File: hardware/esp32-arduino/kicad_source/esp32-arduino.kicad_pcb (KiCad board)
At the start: 2 copper layers, 72 x 53 mm, 52 parts, among them CN1 ARDUINO, Q1 Q_NMOS_GSD, SW1 TAST_HOR, SW2 TAST_HOR, SW3 TAST_HOR, SW4 TAST_HOR, SW5 TAST_HOR, SW6 TAST_HOR, U1 LT1117, U2 TLV733P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

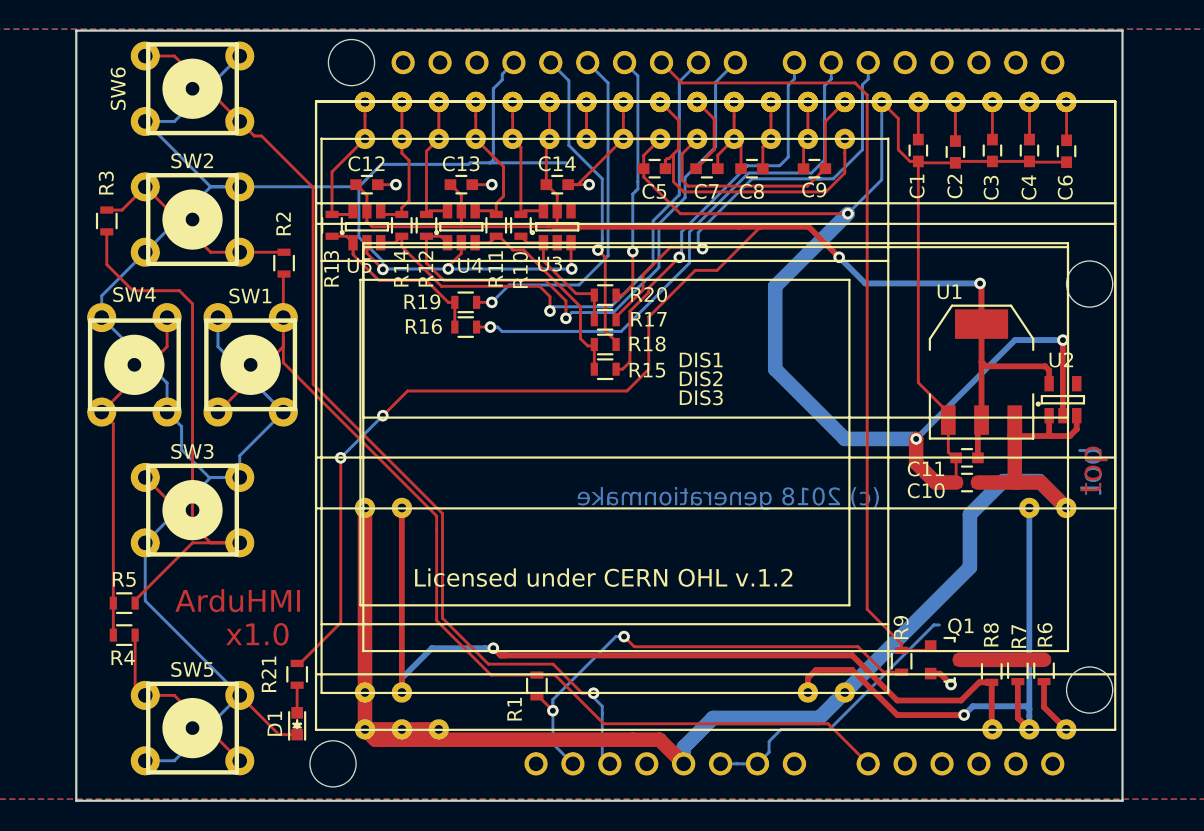
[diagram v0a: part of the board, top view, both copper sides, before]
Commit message: started schematic added ESP32
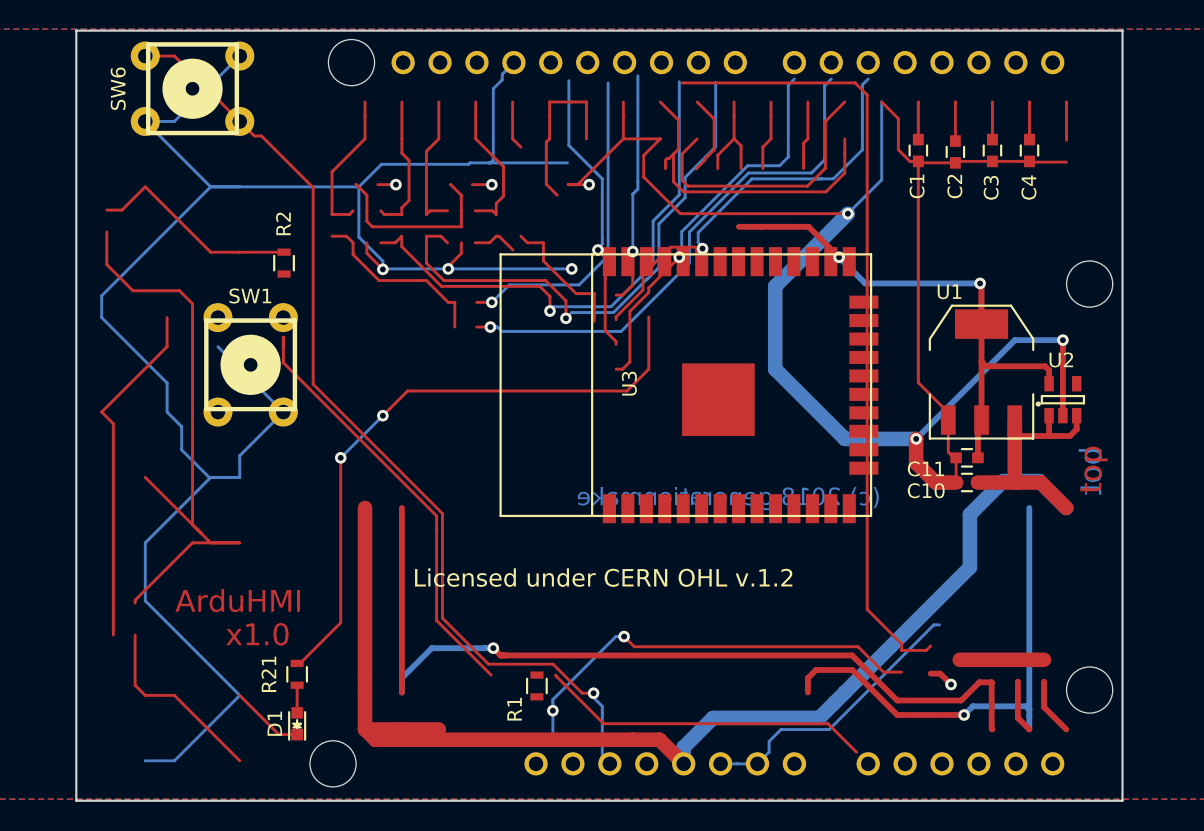
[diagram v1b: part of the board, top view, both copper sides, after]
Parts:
- removed C12, C13, C14: 100n, capacitors:C_0603
- removed C5, C6, C7, C8, C9: 1u, capacitors:C_0603
- removed DIS1: EA_DOGM128-6, displays:EA_DOGM128
- removed DIS2: EA_DOGM132-5, displays:EA_DOGM081_162_163_132
- removed DIS3: EA_DOGS102-6, displays:EA_DOGS102
- removed Q1: Q_NMOS_GSD, SOT_TO:SOT-23
- removed R10, R11, R12, R13, R14, R15, R16, R17: DNI, resistors:R_0603
- removed R18, R19, R20: 0R, resistors:R_0603
- removed R3: 620, resistors:R_0603
- removed R4, R9: 1k, resistors:R_0603
- removed R5: 3k3, resistors:R_0603
- removed R6, R7, R8: 30, resistors:R_0603
- removed SW2, SW3, SW4, SW5: TAST_HOR, mechanical-switches:PCB_PUSH
- removed U4, U5: SN74LVC2G34, SOT_TO:SOT-23-6
- C1, C2, C4: value 1u -> 100n
- C3: value 1u -> 10u
- R1: value 2k -> 1k
- R2: value 330 -> 1k
- SW1: value TAST_HOR -> SW_PUSH
- U3: value SN74LVC2G34 -> ESP32_WROOM_32; footprint SOT_TO:SOT-23-6 -> MODULE_compute:ESP32-WROOM-32
- moved U3 15.6 mm to (95.2, 101.4)
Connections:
- C1 pad 1: /DIS_V4 -> /RESET
- C10 pad 1: +5V -> VIN
- C2 pad 1: /DIS_V3 -> +3V3
- C3 pad 1: /DIS_V2 -> +3V3
- C4 pad 1: /DIS_V1 -> +3V3
- CN1 pad 0: Net-(CN1-Pad0) -> (no net)
- CN1 pad 1: Net-(CN1-Pad1) -> (no net)
- CN1 pad 10: /DISPLAY_BL -> (no net)
- CN1 pad 11: /ARDU_SI_1 -> (no net)
- CN1 pad 12: /ARDU_CS_1 -> (no net)
- CN1 pad 13: /ARDU_CLK_1 -> (no net)
- CN1 pad 15: Net-(CN1-Pad15) -> (no net)
- CN1 pad 16: Net-(CN1-Pad16) -> (no net)
- CN1 pad 17: Net-(CN1-Pad17) -> (no net)
- CN1 pad 18: /ENC_SW -> (no net)
- CN1 pad 19: /ENC_B -> (no net)
- CN1 pad 2: Net-(CN1-Pad2) -> (no net)
- CN1 pad 20: /ENC_A -> (no net)
- CN1 pad 21: Net-(CN1-Pad21) -> (no net)
- CN1 pad 22: Net-(CN1-Pad22) -> (no net)
- CN1 pad 23: /KEYPAD_A0 -> (no net)
- CN1 pad 27: +5V -> Net-(CN1-Pad27)
- CN1 pad 28: Net-(CN1-Pad28) -> +3V3
- CN1 pad 3: Net-(CN1-Pad3) -> (no net)
- CN1 pad 30: VIO -> +3V3
- CN1 pad 31: Net-(CN1-Pad31) -> (no net)
- CN1 pad 4: Net-(CN1-Pad4) -> (no net)
- CN1 pad 5: /ARDU_SI_2 -> (no net)
- CN1 pad 6: /ARDU_CS_2 -> (no net)
- CN1 pad 7: /ARDU_CLK_2 -> (no net)
- CN1 pad 8: /ARDU_A0 -> (no net)
- CN1 pad 9: /ARDU_RESET -> (no net)
- R1 pad 1: VIO -> /RESET
- R1 pad 2: /KEYPAD_A0 -> +3V3
- R2 pad 1: /KEYPAD_A0 -> Net-(CN1-Pad27)
- R2 pad 2: /BUTTON_UP -> VIN
- SW1 pad 1: GND -> /BOOT
- SW1 pad 3: /KEYPAD_A0 -> (no net)
- SW1 pad 4: /KEYPAD_A0 -> (no net)
- U1 pad 3: +5V -> VIN
- U2 pad 1: +5V -> VIN
- U2 pad 3: +5V -> VIN
- U2 pad 4: Net-(U2-Pad4) -> (no net)
- U3 pad 1: /ARDU_SI -> GND
- U3 pad 2: GND -> +3V3
- U3 pad 3: GND -> /RESET
- U3 pad 4: Net-(U3-Pad4) -> (no net)
- U3 pad 5: +3V3 -> (no net)
- U3 pad 6: /DIS_SI -> (no net)
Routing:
- net +5V: track 118.3 -> 0.00 mm
- net (no net): track 0.00 -> 108.1 mm, vias 0 -> 3
- net Net-(CN1-Pad27): track 0.00 -> 100.3 mm
- net +3V3: track 162.7 -> 109.1 mm
- net VIN: track 0.32 -> 33.0 mm
- net /ARDU_SI_2: track 30.2 -> 0.00 mm, vias 1 -> 0
- net /ARDU_CLK_2: track 27.9 -> 0.00 mm, vias 1 -> 0
- net GND: track 302.4 -> 326.8 mm, vias 10 -> 11
- net /ARDU_CLK_1: track 21.6 -> 0.00 mm, vias 1 -> 0
- net /DIS_CAP2N: track 18.9 -> 0.00 mm
- net /ARDU_SI_1: track 17.3 -> 0.00 mm, vias 1 -> 0
- net /KEYPAD_A0: track 69.1 -> 52.8 mm
- net /BUTTON_UP: track 14.7 -> 0.00 mm
- net /ARDU_CLK: track 14.5 -> 3.18 mm
- net /ARDU_SI: track 9.32 -> 0.00 mm
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
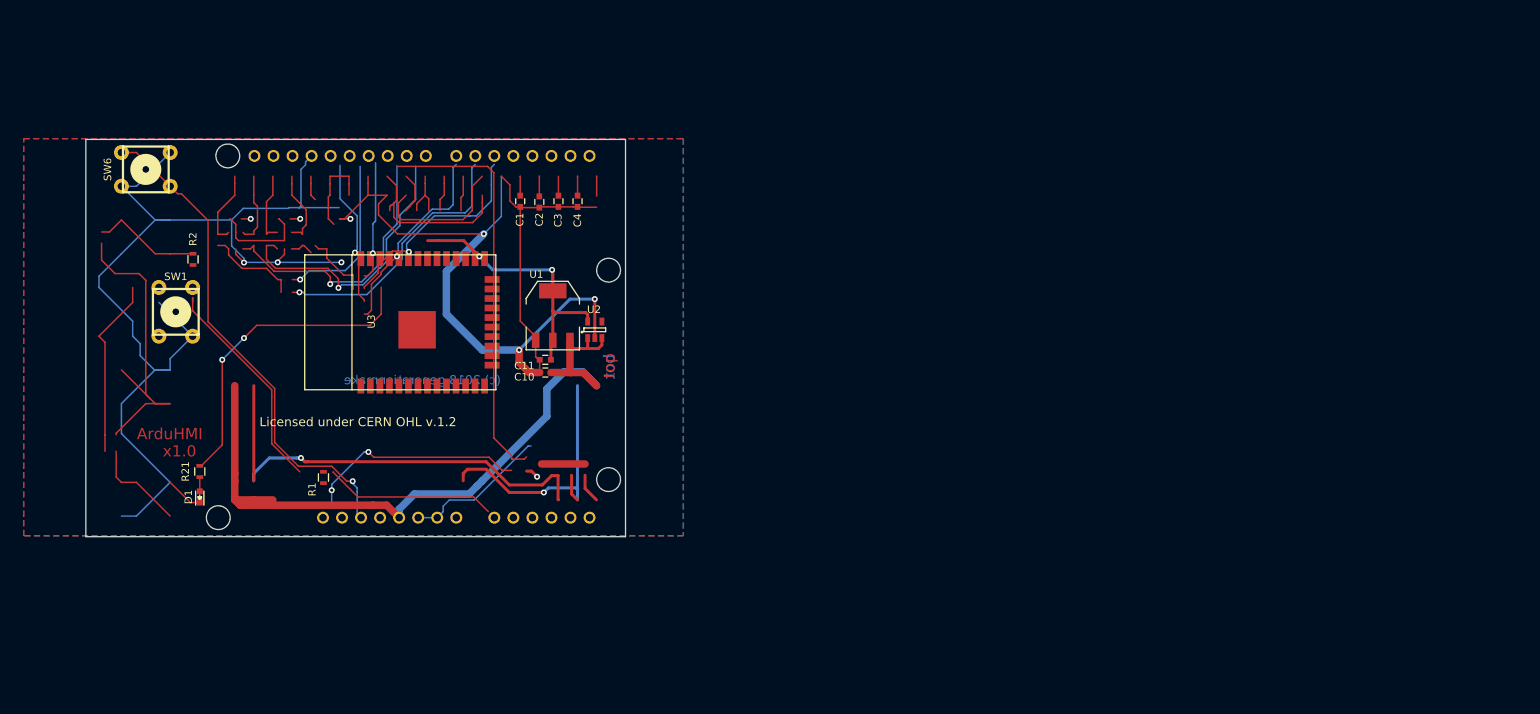
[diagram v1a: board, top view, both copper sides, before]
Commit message: corrected schematic, updated layout
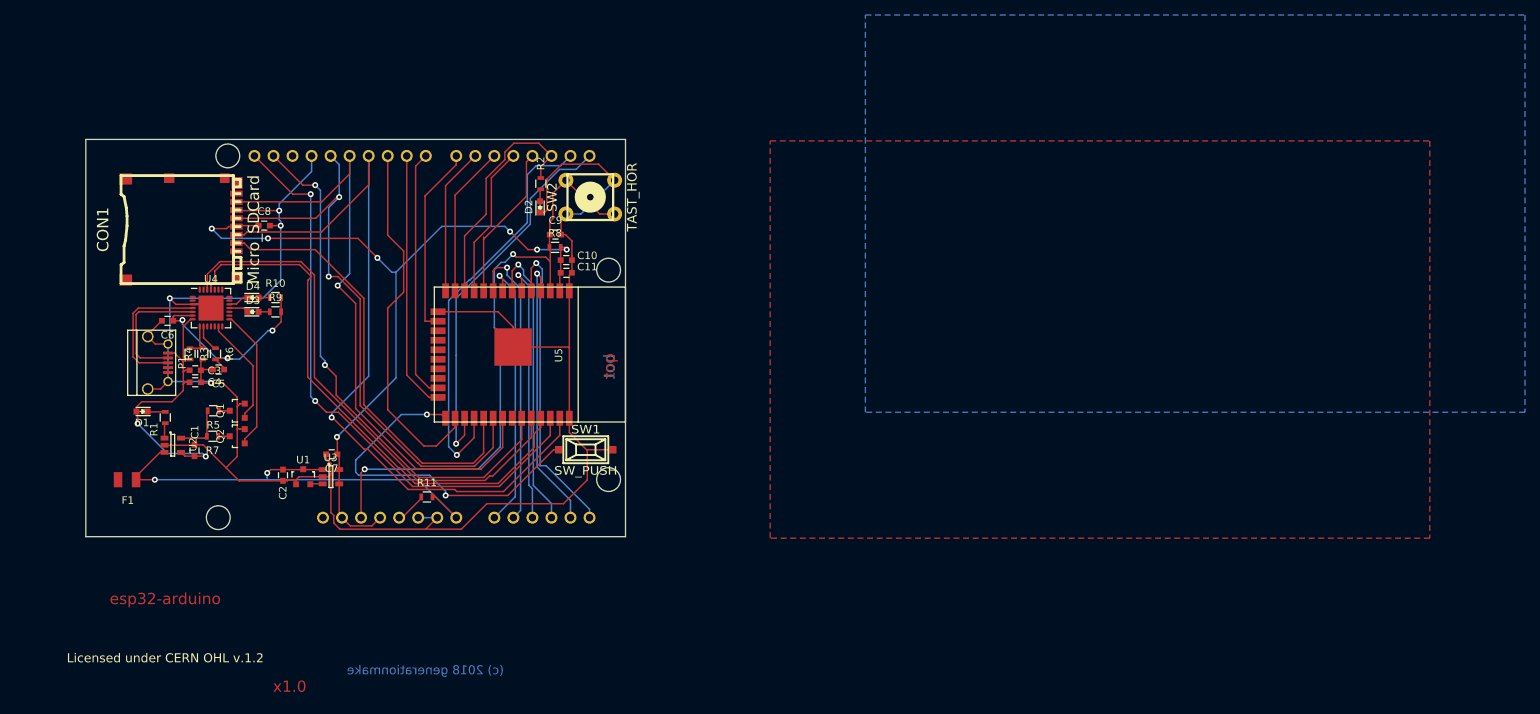
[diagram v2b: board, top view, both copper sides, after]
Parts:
- removed R21: 1k, resistors:R_0603
- removed SW6: TAST_HOR, mechanical-switches:PCB_PUSH
- added C5: 10u, capacitors:C_0603, F.Cu at (68.7, 107.7)
- added C6: 100n, capacitors:C_0603, F.Cu at (61.9, 101.2)
- added C7: 1u, capacitors:C_0603, F.Cu at (83.8, 119.0)
- added C8: 100n, capacitors:C_0603, F.Cu at (74.8, 88.5)
- added C9: 100n, capacitors:C_0603, F.Cu at (113.7, 89.7)
- added CON1: Micro_SDCard, mechanical-connectors:microsd_socket, F.Cu at (63.3, 90.6)
- added D2: green, LEDs:LED_0603, F.Cu at (111.6, 86.0)
- added D3: green, LEDs:LED_0603, F.Cu at (73.3, 100.0)
- added D4: green, LEDs:LED_0603, F.Cu at (73.3, 98.1)
- added F1: F_Small, fuse_holders_and_fuses:Fuse_SMD1206_Reflow, F.Cu at (56.5, 122.4)
- added P1: USB_OTG, mechanical-connectors:USB_Micro-B, F.Cu at (60.4, 106.8)
- added Q1: Q_NMOS_GSD, SOT_TO:SOT-23, F.Cu at (71.2, 113.2)
- added Q2: Q_NMOS_GSD, SOT_TO:SOT-23, F.Cu at (71.2, 116.6)
- added R10: 1k, resistors:R_0603, F.Cu at (76.3, 98.1)
- added R11: 1k, resistors:R_0603, F.Cu at (96.5, 124.7)
- added R3: 22k1, resistors:R_0603, F.Cu at (64.9, 105.6)
- added R4: 47k5, resistors:R_0603, F.Cu at (66.6, 105.6)
- added R5: 1k, resistors:R_0603, F.Cu at (68.0, 113.2)
- added R6: 1k, resistors:R_0603, F.Cu at (68.3, 105.6)
- added R7: 1k, resistors:R_0603, F.Cu at (67.9, 116.6)
- added R8: 1k, resistors:R_0603, F.Cu at (113.6, 91.4)
- added R9: 1k, resistors:R_0603, F.Cu at (76.3, 100.0)
- added SW2: TAST_HOR, mechanical-switches:PCB_PUSH, F.Cu at (118.3, 84.7)
- added U4: CP2102N_28, QFN:QFN-28-1EP_5x5mm_Pitch0.5mm, F.Cu at (67.7, 99.5)
- added U5: ESP32_WROOM_32, MODULE_compute:ESP32-WROOM-32, F.Cu at (108.0, 105.7)
- C1, C2: value 100n -> 1u
- C10: value 1u -> 10u
- C11: value 1u -> 100n
- SW1: footprint mechanical-switches:PCB_PUSH -> mechanical-switches:smd_push
- U1: value LT1117 -> TPS383X; footprint SOT_TO:SOT-223 -> SOT_TO:SOT-23
- U2: value TLV733P -> MCP73831
- U3: value ESP32_WROOM_32 -> TPS736XX; footprint MODULE_compute:ESP32-WROOM-32 -> SOT_TO:SOT-23-5
- moved U2 58.4 mm to (62.6, 117.8), turned to 0 degrees
- moved SW1 57.7 mm to (117.7, 118.4)
- moved C4 56.4 mm to (65.6, 109.4), turned to 0 degrees
- moved C1 54.7 mm to (65.5, 118.5), turned to 90 degrees
- moved C3 53.4 mm to (65.6, 107.8), turned to 0 degrees
- moved C2 50.0 mm to (77.3, 121.8)
- moved R2 47.5 mm to (111.7, 82.9)
- moved U1 39.6 mm to (80.0, 122.0)
- moved U3 23.6 mm to (83.7, 122.0), turned to 0 degrees
- moved R1 22.6 mm to (61.6, 114.1)
- moved C10 15.3 mm to (115.1, 93.1), turned to 0 degrees
- moved D1 13.8 mm to (58.5, 113.3), turned to 180 degrees
- moved C11 11.9 mm to (115.1, 94.8), turned to 0 degrees
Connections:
- C1 pad 1: /RESET -> VIN
- C10 pad 1: VIN -> +3V3
- C2 pad 1: +3V3 -> +BATT
- C3 pad 1: +3V3 -> VIN
- C4 pad 1: +3V3 -> VIN
- CN1 pad 0: (no net) -> /EXT_RX
- CN1 pad 1: (no net) -> /EXT_TX
- CN1 pad 10: (no net) -> /SPI_CS_EXT
- CN1 pad 11: (no net) -> /SPI_MOSI
- CN1 pad 12: (no net) -> /SPI_MISO
- CN1 pad 13: (no net) -> /SPI_CLK
- CN1 pad 16: (no net) -> /I2C_SDA
- CN1 pad 17: (no net) -> /I2C_SCL
- CN1 pad 18: (no net) -> /ADC_5
- CN1 pad 19: (no net) -> /ADC_4
- CN1 pad 2: (no net) -> /ARDUINO_2
- CN1 pad 20: (no net) -> /ADC_3
- CN1 pad 21: (no net) -> /ADC_2
- CN1 pad 22: (no net) -> /ADC_1
- CN1 pad 23: (no net) -> /ADC_0
- CN1 pad 24: VIN -> +BATT
- CN1 pad 3: (no net) -> /DAC_1
- CN1 pad 4: (no net) -> /DAC_2
- CN1 pad 5: (no net) -> /ARDUINO_5
- CN1 pad 6: (no net) -> /ARDUINO_6
- CN1 pad 7: (no net) -> /ARDUINO_7
- CN1 pad 8: (no net) -> /ARDUINO_8
- CN1 pad 9: (no net) -> /ARDUINO_9
- D1 pad 1: GND -> Net-(D1-Pad1)
- D1 pad 2: Net-(D1-Pad2) -> VIN
- R1 pad 1: /RESET -> Net-(R1-Pad1)
- R1 pad 2: +3V3 -> Net-(D1-Pad1)
- R2 pad 1: Net-(CN1-Pad27) -> Net-(D2-Pad2)
- R2 pad 2: VIN -> /ARDUINO_2
- U1 pad 2: +3V3 -> Net-(U1-Pad2)
- U1 pad 3: VIN -> +BATT
- U2 pad 1: VIN -> Net-(R1-Pad1)
- U2 pad 3: VIN -> +BATT
- U2 pad 4: (no net) -> VIN
- U2 pad 5: +3V3 -> Net-(R5-Pad2)
- U3 pad 1: GND -> +BATT
- U3 pad 2: +3V3 -> GND
- U3 pad 3: /RESET -> Net-(U1-Pad2)
- U3 pad 4: (no net) -> +3V3
- U3 pad 5: (no net) -> +3V3
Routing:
- net (no net): track 108.1 -> 0.00 mm, vias 3 -> 0
- net /SPI_MOSI: track 0.00 -> 101.1 mm, vias 0 -> 1
- net Net-(CN1-Pad27): track 100.3 -> 4.57 mm
- net /DIS_C1: track 84.6 -> 0.00 mm, vias 1 -> 0
- net /SPI_MISO: track 0.00 -> 82.5 mm, vias 0 -> 1
- net /I2C_SCL: track 0.00 -> 78.7 mm, vias 0 -> 2
- net /SPI_CLK: track 0.00 -> 77.7 mm, vias 0 -> 2
- net /RX: track 0.00 -> 72.7 mm
- net /TX: track 0.00 -> 72.6 mm
- net /I2C_SDA: track 0.00 -> 70.6 mm, vias 0 -> 2
- net +BATT: track 0.00 -> 63.5 mm, vias 0 -> 2
- net /SPI_CS_SD: track 0.00 -> 58.7 mm
- net GND: track 326.8 -> 270.5 mm, vias 11 -> 4
- net /EXT_TX: track 0.00 -> 54.9 mm, vias 0 -> 1
- net /DISPLAY_BL: track 54.4 -> 0.00 mm
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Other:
- board text added: "esp32-arduino"
- board text removed: "ArduHMI"

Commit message: finished layout, created gerber
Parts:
- added BT1: Battery, MECH_battery_holder:KEYSTONE_1043, B.Cu at (84.1, 115.0)
- added R12: 100R, resistors:R_0603, F.Cu at (107.3, 102.3)
- added R13: 100R, resistors:R_0603, F.Cu at (107.3, 103.7)
- added R14: 100R, resistors:R_0603, F.Cu at (107.3, 105.8)
- added R15: 100R, resistors:R_0603, F.Cu at (107.1, 108.1)
- CON1: footprint mechanical-connectors:microsd_socket -> CON_wuerth:WE_693072010801
- SW1: value SW_PUSH -> TAST_VER; footprint mechanical-switches:smd_push -> mechanical-switches:WE_430182050816
- SW2: value TAST_HOR -> TAST_VER; footprint mechanical-switches:PCB_PUSH -> mechanical-switches:WE_430182050816
- moved C10 69.3 mm to (46.3, 85.1), turned to 90 degrees
- moved C11 67.9 mm to (47.9, 85.0), turned to 90 degrees
- moved U5 51.4 mm to (58.4, 92.0), turned to 0 degrees
- moved C8 48.8 mm to (117.2, 112.7)
- moved CON1 48.1 mm to (109.3, 104.6), turned to 90 degrees
- moved SW1 42.5 mm to (75.9, 126.3)
- moved R8 36.0 mm to (86.1, 114.7), turned to 180 degrees
- moved R10 21.1 mm to (71.5, 118.6), turned to 270 degrees
- moved R9 19.8 mm to (69.6, 118.6), turned to 270 degrees
- moved D4 17.6 mm to (71.5, 115.6), turned to 270 degrees
- moved D3 16.0 mm to (69.6, 115.6), turned to 270 degrees
- moved Q1 11.6 mm to (59.8, 115.1), turned to 180 degrees
- moved P1 11.3 mm to (49.1, 107.6)
- moved U4 10.8 mm to (70.1, 110.0), turned to 270 degrees
- moved D2 10.4 mm to (121.6, 83.2)
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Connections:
- net Net-(R5-Pad2) renamed /PROG
- CON1 pad 2: /SPI_CS_SD -> /SPI_CS_SD_R
- CON1 pad 3: /SPI_MOSI -> /SPI_MOSI_R
- CON1 pad 5: /SPI_CLK -> /SPI_CLK_R
- CON1 pad 7: /SPI_MISO -> /SPI_MISO_R
- F1 pad 2: (no net) -> Net-(BT1-Pad1)
- SW2 pad 2: GND -> /RESET
- SW2 pad 3: /RESET -> GND
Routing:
- net /I2C_SCL: track 78.7 -> 11.4 mm, vias 2 -> 0
- net /ADC_4: track 36.9 -> 95.4 mm
- net /ARDUINO_2: track 31.7 -> 89.9 mm, vias 0 -> 2
- net /ADC_5: track 41.6 -> 99.4 mm
- net /DAC_1: track 21.0 -> 76.6 mm, vias 0 -> 2
- net /ADC_2: track 35.4 -> 90.8 mm
- net /ADC_1: track 39.2 -> 94.5 mm
- net /ADC_3: track 39.5 -> 94.8 mm
- net /ADC_0: track 36.5 -> 89.2 mm
- net /DAC_2: track 20.2 -> 72.0 mm, vias 0 -> 2
- net /ARDUINO_5: track 20.2 -> 69.1 mm, vias 0 -> 2
- net +3V3: track 109.2 -> 157.4 mm, vias 7 -> 3
- net /ARDUINO_6: track 19.6 -> 66.8 mm, vias 0 -> 2
- net GND: track 270.5 -> 317.3 mm, vias 4 -> 5
- net /I2C_SDA: track 70.6 -> 26.8 mm, vias 2 -> 0
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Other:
- board size 72 x 53 mm -> 78 x 53 mm
- board text added: "BOOT"
- board text added: "RESET"

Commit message: corrected schematic and layout, generated gerber
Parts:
- added R16: 1k, resistors:R_0603, F.Cu at (76.6, 111.8)
- added R17: 1k, resistors:R_0603, F.Cu at (76.6, 109.8)
- added R18: 1k, resistors:R_0603, F.Cu at (73.2, 83.3)
- added R19: 1k, resistors:R_0603, F.Cu at (77.2, 83.3)
- added R20: 1k, resistors:R_0603, F.Cu at (104.9, 125.1)
- added R21: 1k, resistors:R_0603, F.Cu at (108.1, 125.1)
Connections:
- U4 pad 25: /TX -> /TX_R
- U4 pad 26: /RX -> /RX_R
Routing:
- net +3V3: track 157.4 -> 192.1 mm, vias 3 -> 4
- net GND: track 317.3 -> 305.0 mm, vias 5 -> 24
- net /TX: track 50.3 -> 44.8 mm
- net /RX: track 46.2 -> 41.3 mm
- net /ADC_1: track 94.5 -> 98.9 mm
- net /TX_R: track 0.00 -> 4.16 mm
- net +BATT: track 77.7 -> 81.9 mm
- net /RX_R: track 0.00 -> 3.42 mm
- net /I2C_SDA: track 26.8 -> 28.6 mm
- net VIN: track 52.6 -> 53.5 mm
- net /I2C_SCL: track 11.4 -> 12.0 mm
